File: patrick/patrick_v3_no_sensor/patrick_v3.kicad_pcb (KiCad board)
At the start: 2 copper layers, 21 x 13 mm, 13 parts, among them J1 Conn_01x10, Q1 Q_NMOS_GSD, Q2 Q_NMOS_GSD, Q3 Q_NMOS_GSD, Q4 Q_NMOS_GSD

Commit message: modified patrick boards
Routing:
- net Net-(J1-Pad8): track 8.80 -> 16.1 mm
- net /+12V: track 2.90 -> 8.27 mm

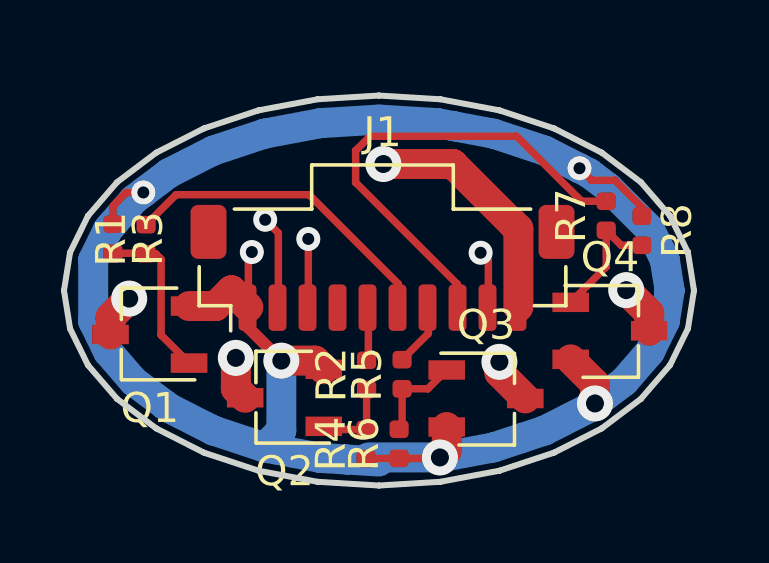
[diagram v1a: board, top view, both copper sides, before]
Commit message: minigrid connectors instead of picoclasp
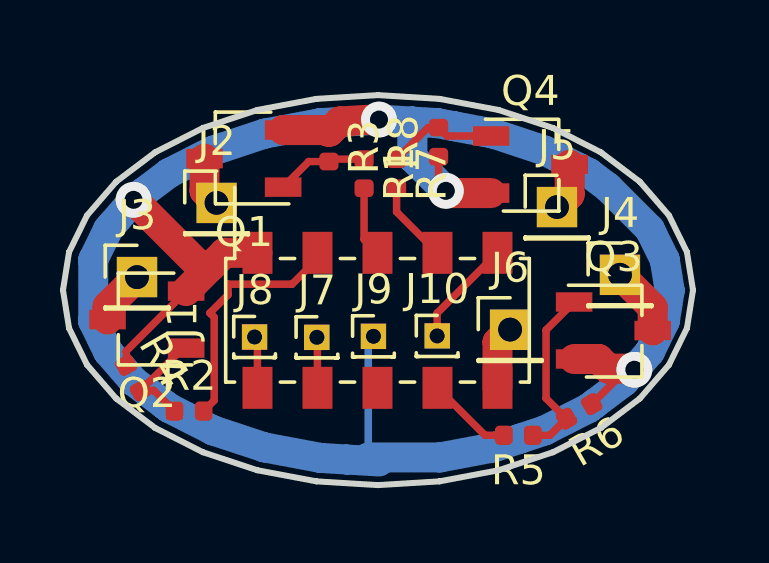
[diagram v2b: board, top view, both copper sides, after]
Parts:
- added J10: Conn_01x01, Connector_PinHeader_1.00mm:PinHeader_1x01_P1.00mm_Vertical, F.Cu at (157.4, 108.6)
- added J2: Conn_01x01, Connector_PinHeader_2.00mm:PinHeader_1x01_P2.00mm_Vertical, F.Cu at (150.0, 104.2)
- added J3: Conn_01x01, Connector_PinHeader_2.00mm:PinHeader_1x01_P2.00mm_Vertical, F.Cu at (147.4, 106.7)
- added J4: Conn_01x01, Connector_PinHeader_2.00mm:PinHeader_1x01_P2.00mm_Vertical, F.Cu at (163.5, 106.6)
- added J5: Conn_01x01, Connector_PinHeader_2.00mm:PinHeader_1x01_P2.00mm_Vertical, F.Cu at (161.4, 104.3)
- added J6: Conn_01x01, Connector_PinHeader_2.00mm:PinHeader_1x01_P2.00mm_Vertical, F.Cu at (159.8, 108.4)
- added J7: Conn_01x01, Connector_PinHeader_1.00mm:PinHeader_1x01_P1.00mm_Vertical, F.Cu at (153.4, 108.7)
- added J8: Conn_01x01, Connector_PinHeader_1.00mm:PinHeader_1x01_P1.00mm_Vertical, F.Cu at (151.3, 108.7)
- added J9: Conn_01x01, Connector_PinHeader_1.00mm:PinHeader_1x01_P1.00mm_Vertical, F.Cu at (155.2, 108.6)
- J1: value Conn_01x10 -> Conn_02x05_Counter_Clockwise; footprint MolexPicoClasp:Molex_Pico-Clasp_501331-1007_1x10-1MP_P1.00mm_Vertical -> molex_791091004:PinSocket_2x05_P2.00mm_Vertical_SMD
- moved R4 8.06 mm to (147.2, 110.0), turned to 300 degrees
- moved R3 7.82 mm to (153.8, 102.3)
- moved R1 7.59 mm to (154.9, 103.2), turned to 270 degrees
- moved R8 7.39 mm to (157.4, 102.2), turned to 90 degrees
- moved R7 7.13 mm to (156.0, 103.2), turned to 270 degrees
- moved Q1 6.65 mm to (150.9, 102.7)
- moved Q4 6.15 mm to (160.5, 102.9)
- moved R6 6.09 mm to (162.1, 111.1), turned to 210 degrees
- moved R2 6.04 mm to (149.1, 111.1), turned to 0 degrees
- moved Q2 5.28 mm to (147.7, 108.1)
- moved Q3 4.81 mm to (163.2, 108.4)
- moved R5 4.38 mm to (160.1, 111.9), turned to 180 degrees
- moved J1 1.76 mm to (155.4, 108.1), turned to 90 degrees
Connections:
- J1 pad 2: /SCL -> /SDA
- J1 pad 3: /SDA -> Net-(J1-Pad3)
- J1 pad 4: Net-(J1-Pad4) -> /SCL
- R1 pad 2: Net-(J1-Pad6) -> Net-(J1-Pad5)
- R2 pad 2: Net-(J1-Pad5) -> Net-(J1-Pad3)
- R5 pad 2: Net-(J1-Pad7) -> Net-(J1-Pad8)
- R7 pad 2: Net-(J1-Pad8) -> Net-(J1-Pad7)
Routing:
- net Net-(J1-Pad8): track 16.1 -> 2.87 mm
- net Net-(J1-Pad6): track 10.8 -> 0.00 mm
- net Net-(J1-Pad3): track 0.00 -> 8.22 mm
- net /+12V: track 8.27 -> 2.11 mm, vias 1 -> 0
- net GND: track 70.7 -> 76.1 mm, vias 6 -> 4
- net Net-(Q3-Pad1): track 3.14 -> 5.91 mm
- net Net-(Q1-Pad1): track 5.54 -> 3.08 mm
- net /SCL: track 3.32 -> 1.69 mm, vias 1 -> 0
- net +3V3: track 2.03 -> 3.60 mm, vias 1 -> 0
- net Net-(J4-Pad1): track 1.58 -> 2.31 mm, vias 1 -> 0
- net Net-(Q2-Pad1): track 2.79 -> 3.51 mm
- net Net-(J1-Pad7): track 2.11 -> 2.72 mm
- net Net-(Q4-Pad1): track 4.29 -> 3.70 mm
- net /SDA: track 2.28 -> 1.73 mm, vias 1 -> 0
- net Net-(J1-Pad5): track 1.79 -> 2.34 mm
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
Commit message: added patrick board with bigger vias for battery wires
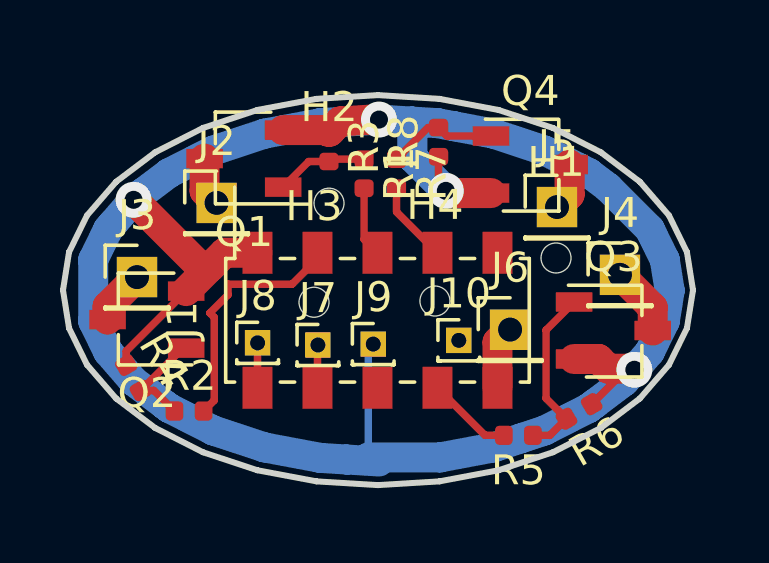
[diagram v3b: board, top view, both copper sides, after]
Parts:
- added H1: MountingHole, MountingHole:MountingHole_2mm, F.Cu at (161.3, 106.0)
- added H2: MountingHole, MountingHole:MountingHole_2mm, F.Cu at (153.8, 104.2)
- added H3: MountingHole, MountingHole:MountingHole_2mm, F.Cu at (153.3, 107.5)
- added H4: MountingHole, MountingHole:MountingHole_2mm, F.Cu at (157.3, 107.5)
- moved J10 0.74 mm to (158.1, 108.8)
- moved J9 0.26 mm to (155.2, 108.9)
- moved J7 0.26 mm to (153.4, 108.9)
- moved J8 0.22 mm to (151.4, 108.9)
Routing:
- net +3V3: track 3.60 -> 0.00 mm
